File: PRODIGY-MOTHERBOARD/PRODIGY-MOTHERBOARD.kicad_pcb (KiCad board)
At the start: 2 copper layers, 204 parts, among them J10 GPIO, J11 SPI_OUT, J12 I2C, J13 CAN, J14 SERIAL, J15 12V OUT, J16 SERVO, J17 SERVO, J18 SERVO, J19 Ultrasonic, J20 MOTOR, J21 MOTOR, J22 DM3BT-DSF-PEJS/C, J23 Barrel_Jack_MountingPin, J26 KEYPAD_MATRIX, J28 AudioJack4, J4 USB_A, J5 A_OUT, J6 Neopixel, J7 GPIO, J8 GPIO, J9 GPIO, P1 USB_C_Plug, Q1 DMP2045U-7, Q2 BC850, Q3 BC850, Q4 BS870, Q5 BC850, Q6 ALS-PDIC15-21B/TR8, U10 TJA1051T-E, U11 DRV8870DDA, U12 DRV8870DDA, U13 PCA9306DC, U14 SN74LVC1T45DBV, U15 TXS0108EPW, U16 CR2013-MI2120, U17 PCF8574, U18 PCF8574, U19 HDC1080, U2 CC56-12YWA, U20 LIS2DH12TR, U21 MCP6021RT-E/OT, U22 SN74LVC1T45DBV, U23 TSDP341xx, U25 LMH6559, U3 PN5321A3HN_C1xx, U4 IP4252CZ16, U5 TPS22810DRV, U6 TPS54331DR, U7 TPS54331DR, U8 Si4460, U9 LM386

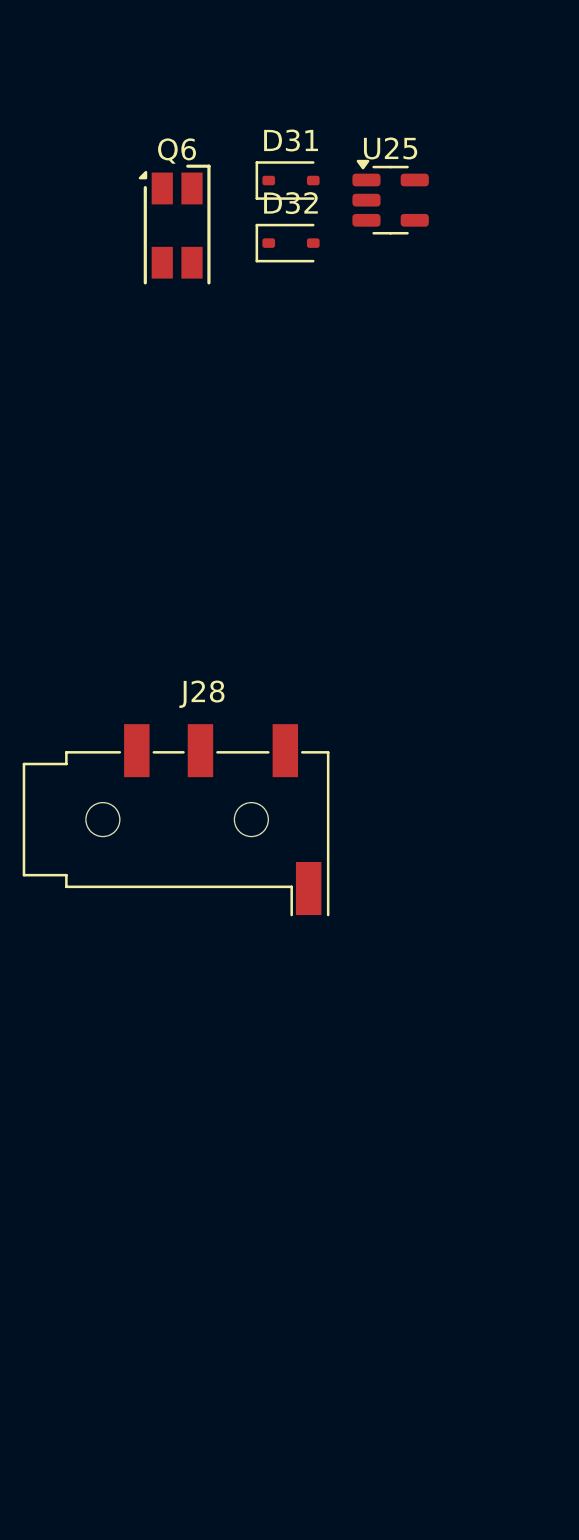
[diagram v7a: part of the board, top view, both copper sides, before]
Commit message: 2-axis joystick footprint and sybmbol created. Analog-side done.
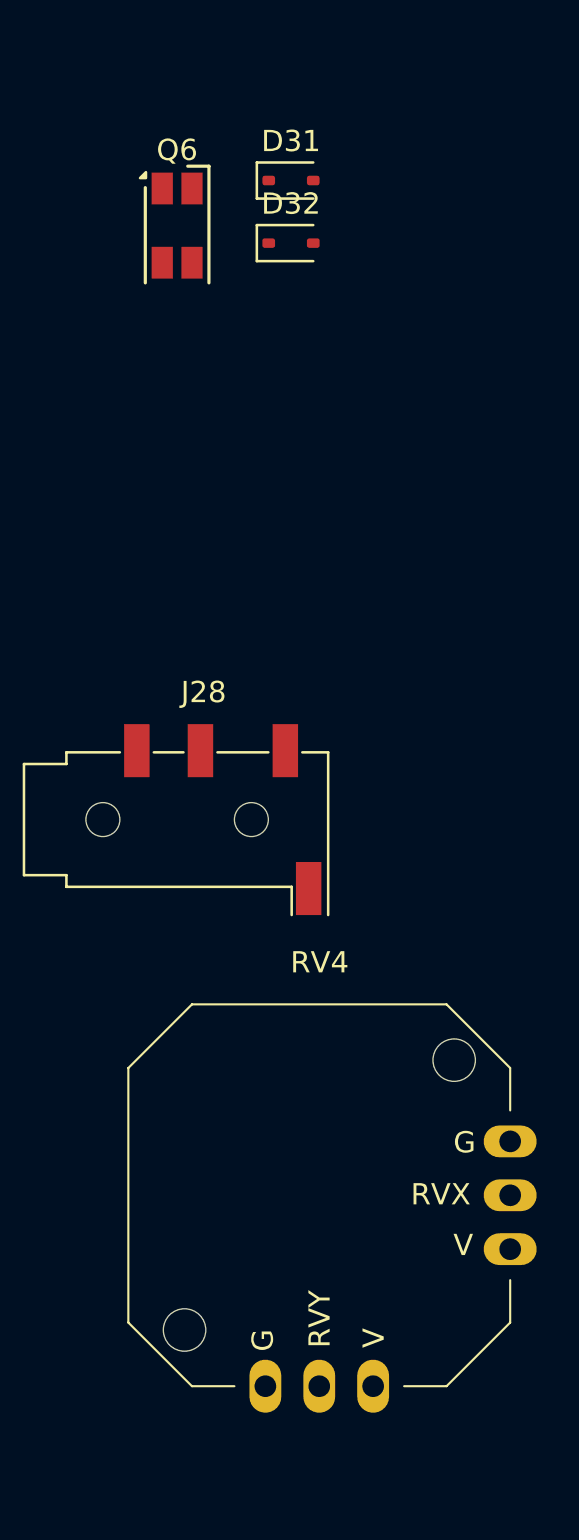
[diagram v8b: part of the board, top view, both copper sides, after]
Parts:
- removed U25: LMH6559, Package_TO_SOT_SMD:SOT-23-5
- added RV4: 10k, potentiometer_2_axis_joystick:2-Axis-Joystick, F.Cu at (185.0, 117.5)
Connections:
- D32 pad 2: Net-(D32-A2) -> /analog/ANALOG_THERMISTOR_OUT
- TH1 pad 2: Net-(D32-A2) -> /analog/ANALOG_THERMISTOR_OUT
